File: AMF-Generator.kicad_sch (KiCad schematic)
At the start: 37 parts, among them J1 SW_OUT, J2 CUR_SENSE, J3 PWR_IN, Q1 ISC012N04LM6ATMA1, Q2 ISC012N04LM6ATMA1, U1 ACS732KLATR-75AB, U2 UCC21540, U8 74LVC1G06

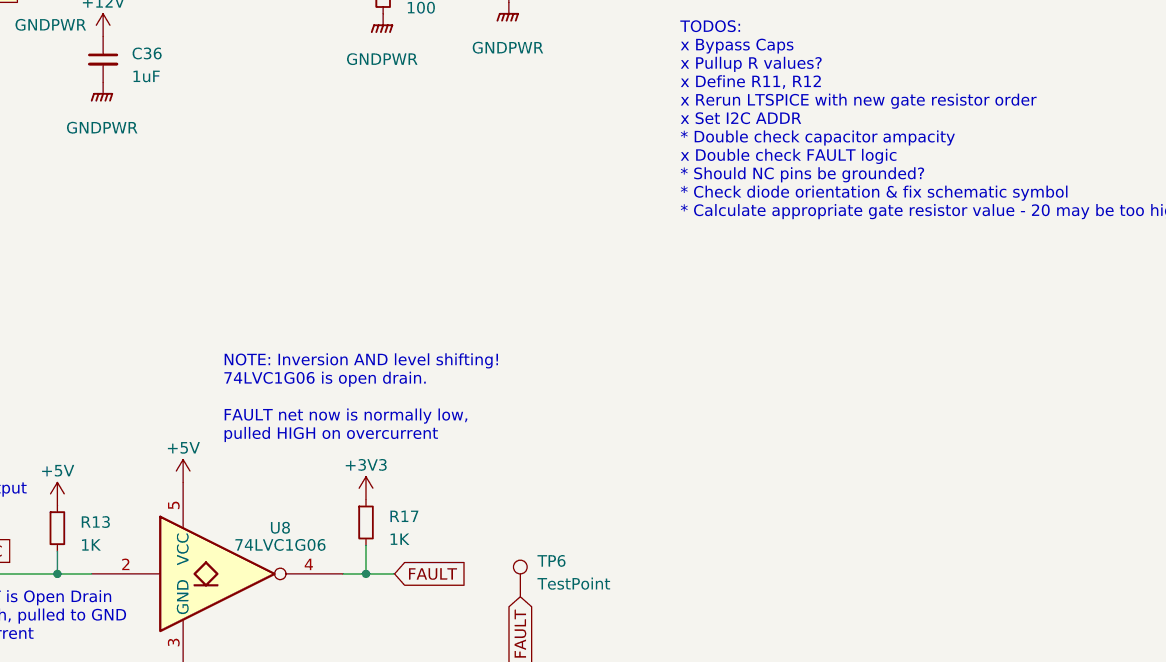
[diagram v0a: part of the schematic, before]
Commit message: Added bypass cap to inverter and some cleanup
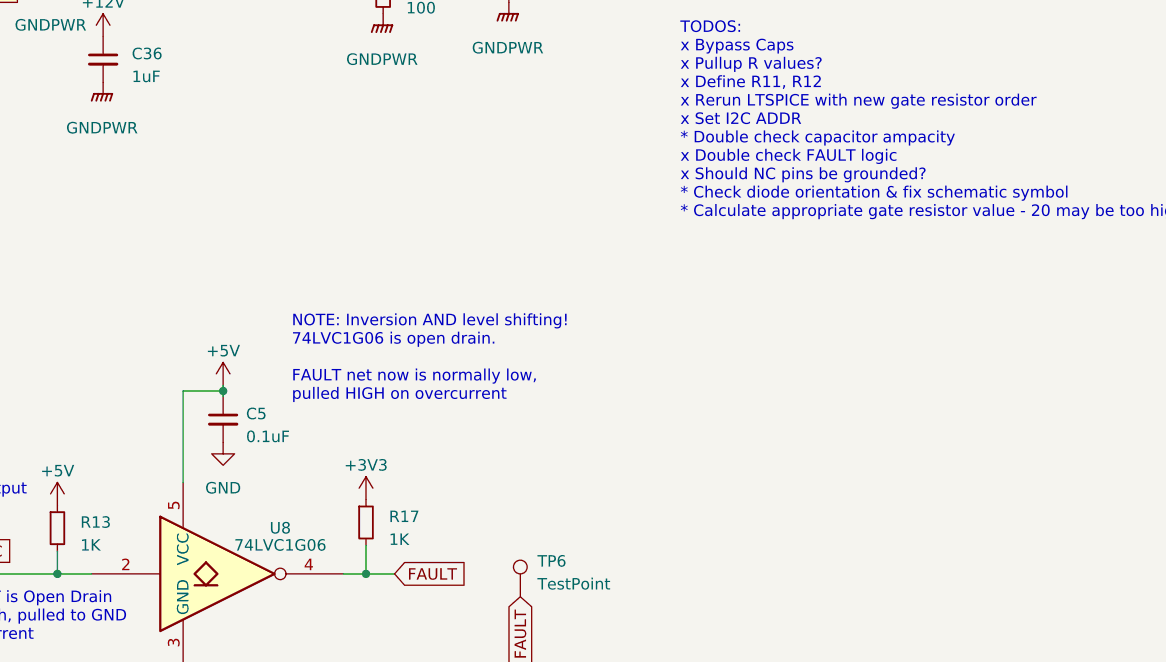
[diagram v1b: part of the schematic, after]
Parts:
- added C5: 0.1uF, Capacitor_SMD:C_0805_2012Metric, symbol Device:C_Small
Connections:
- net +5V: now also C5.1
- net GND: now also C5.2
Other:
- note added: "TODOS: x Bypass Caps x Pullup R values? x Define R11, R12 x Rerun LTSPICE with new gate resistor order x Set I2C ADDR * Double check capacitor ampacity x Double check FAULT logic x Should NC pins be grounded? * Check diode orientation & fix schematic symbol * Calculate appropriate gate resistor value - 20 may be too high"
- note removed: "TODOS: x Bypass Caps x Pullup R values? x Define R11, R12 x Rerun LTSPICE with new gate resistor order x Set I2C ADDR * Double check capacitor ampacity x Double check FAULT logic * Should NC pins be grounded? * Check diode orientation & fix schematic symbol * Calculate appropriate gate resistor value - 20 may be too high"
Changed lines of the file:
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@@
   (junction (at 121.285 166.37) (diameter 0) (color 0 0 0 0)
   )
+  (junction (at 105.41 146.05) (diameter 0) (color 0 0 0 0)
+  )
   (junction (at 143.51 77.47) (diameter 0) (color 0 0 0 0)
   )
@@
     (stroke (width 0) (type default))
   )
+  (wire (pts (xy 100.965 156.21) (xy 100.965 146.05))
+    (stroke (width 0) (type default))
+  )
   (wire (pts (xy 130.81 72.39) (xy 132.08 72.39))
     (stroke (width 0) (type default))
@@
     (stroke (width 0) (type default))
   )
+  (wire (pts (xy 105.41 146.05) (xy 105.41 146.685))
+    (stroke (width 0) (type default))
+  )
   (wire (pts (xy 178.435 77.47) (xy 178.435 69.85))
     (stroke (width 0) (type default))
@@
     (stroke (width 0) (type default))
   )
+  (wire (pts (xy 100.965 146.05) (xy 105.41 146.05))
+    (stroke (width 0) (type default))
+  )
   (wire (pts (xy 123.19 97.79) (xy 129.54 97.79))
     (stroke (width 0) (type default))
@@
   )
   (wire (pts (xy 60.325 140.97) (xy 60.325 153.67))
+    (stroke (width 0) (type default))
+  )
+  (wire (pts (xy 105.41 145.415) (xy 105.41 146.05))
     (stroke (width 0) (type default))
   )
@@
     (effects (font (size 1.27 1.27)) (justify left bottom))
   )
-  (text "TODOS:\nx Bypass Caps\nx Pullup R values?\nx Define R11, R12\nx Rerun LTSPICE with new gate resistor order\nx Set I2C ADDR\n* Double check capacitor ampacity\nx Double check FAULT logic\n* Should NC pins be grounded?\n* Check diode orientation & fix schematic symbol\n* Calculate appropriate gate resistor value - 20 may be too high"
+  (text "TODOS:\nx Bypass Caps\nx Pullup R values?\nx Define R11, R12\nx Rerun LTSPICE with new gate resistor order\nx Set I2C ADDR\n* Double check capacitor ampacity\nx Double check FAULT logic\nx Should NC pins be grounded?\n* Check diode orientation & fix schematic symbol\n* Calculate appropriate gate resistor value - 20 may be too high"
     (at 156.21 127 0)
     (effects (font (size 1.27 1.27)) (justify left bottom))
@@
   )
   (text "NOTE: Inversion AND level shifting!\n74LVC1G06 is open drain.\n\nFAULT net now is normally low,\npulled HIGH on overcurrent"
-    (at 105.41 151.765 0)
+    (at 113.03 147.32 0)
     (effects (font (size 1.27 1.27)) (justify left bottom))
   )
@@
         (path "/c3df021c-646c-4a68-ac14-a081c2121d02"
           (reference "#PWR069") (unit 1)
+        )
+      )
+    )
+  )
+  (symbol (lib_id "power:GND") (at 105.41 151.765 0) (unit 1)
+    (in_bom yes) (on_board yes) (dnp no) (fields_autoplaced)
+    (property "Reference" "#PWR065" (at 105.41 158.115 0)
+      (effects (font (size 1.27 1.27)) hide)
+    )
+    (property "Value" "GND" (at 105.41 156.845 0)
+      (effects (font (size 1.27 1.27)))
+    )
+    (property "Footprint" "" (at 105.41 151.765 0)
+      (effects (font (size 1.27 1.27)) hide)
+    )
+    (property "Datasheet" "" (at 105.41 151.765 0)
+      (effects (font (size 1.27 1.27)) hide)
+    )
+    (pin "1")
+    (instances
+      (project "AMF-Generator"
+        (path "/c3df021c-646c-4a68-ac14-a081c2121d02"
+          (reference "#PWR065") (unit 1)
         )
       )
@@
         (path "/c3df021c-646c-4a68-ac14-a081c2121d02"
           (reference "#FLG01") (unit 1)
-        )
-      )
-    )
-  )
-  (symbol (lib_id "power:+5V") (at 100.965 156.21 0) (unit 1)
-    (in_bom yes) (on_board yes) (dnp no) (fields_autoplaced)
-    (property "Reference" "#PWR078" (at 100.965 160.02 0)
-      (effects (font (size 1.27 1.27)) hide)
-    )
-    (property "Value" "+5V" (at 100.965 152.4 0)
-      (effects (font (size 1.27 1.27)))
-    )
-    (property "Footprint" "" (at 100.965 156.21 0)
-      (effects (font (size 1.27 1.27)) hide)
-    )
-    (property "Datasheet" "" (at 100.965 156.21 0)
-      (effects (font (size 1.27 1.27)) hide)
-    )
-    (pin "1")
-    (instances
-      (project "AMF-Generator"
-        (path "/c3df021c-646c-4a68-ac14-a081c2121d02"
-          (reference "#PWR078") (unit 1)
         )
       )
@@
     )
   )
+  (symbol (lib_id "Device:C_Small") (at 105.41 149.225 0) (unit 1)
+    (in_bom yes) (on_board yes) (dnp no) (fields_autoplaced)
+    (property "Reference" "C5" (at 107.95 148.5963 0)
+      (effects (font (size 1.27 1.27)) (justify left))
+    )
+    (property "Value" "0.1uF" (at 107.95 151.1363 0)
+      (effects (font (size 1.27 1.27)) (justify left))
+    )
+    (property "Footprint" "Capacitor_SMD:C_0805_2012Metric" (at 105.41 149.225 0)
+      (effects (font (size 1.27 1.27)) hide)
+    )
+    (property "Datasheet" "~" (at 105.41 149.225 0)
+      (effects (font (size 1.27 1.27)) hide)
+    )
+    (pin "1")
+    (pin "2")
+    (instances
+      (project "AMF-Generator"
+        (path "/c3df021c-646c-4a68-ac14-a081c2121d02"
+          (reference "C5") (unit 1)
+        )
+      )
+    )
+  )
   (symbol (lib_id "power:GNDPWR") (at 92.075 111.76 0) (unit 1)
     (in_bom yes) (on_board yes) (dnp no) (fields_autoplaced)
@@
         )
       )
+    )
+  )
+  (symbol (lib_id "power:+5V") (at 105.41 145.415 0) (unit 1)
+    (in_bom yes) (on_board yes) (dnp no) (fields_autoplaced)
+    (property "Reference" "#PWR064" (at 105.41 149.225 0)
+      (effects (font (size 1.27 1.27)) hide)
+    )
+    (property "Value" "+5V" (at 105.41 141.605 0)
+      (effects (font (size 1.27 1.27)))
+    )
+    (property "Footprint" "" (at 105.41 145.415 0)
+      (effects (font (size 1.27 1.27)) hide)
+    )
+    (property "Datasheet" "" (at 105.41 145.415 0)
+      (effects (font (size 1.27 1.27)) hide)
+    )
+    (pin "1")
+    (instances
+      (project "AMF-Generator"
+        (path "/c3df021c-646c-4a68-ac14-a081c2121d02"
+          (reference "#PWR064") (unit 1)
+        )
+      )

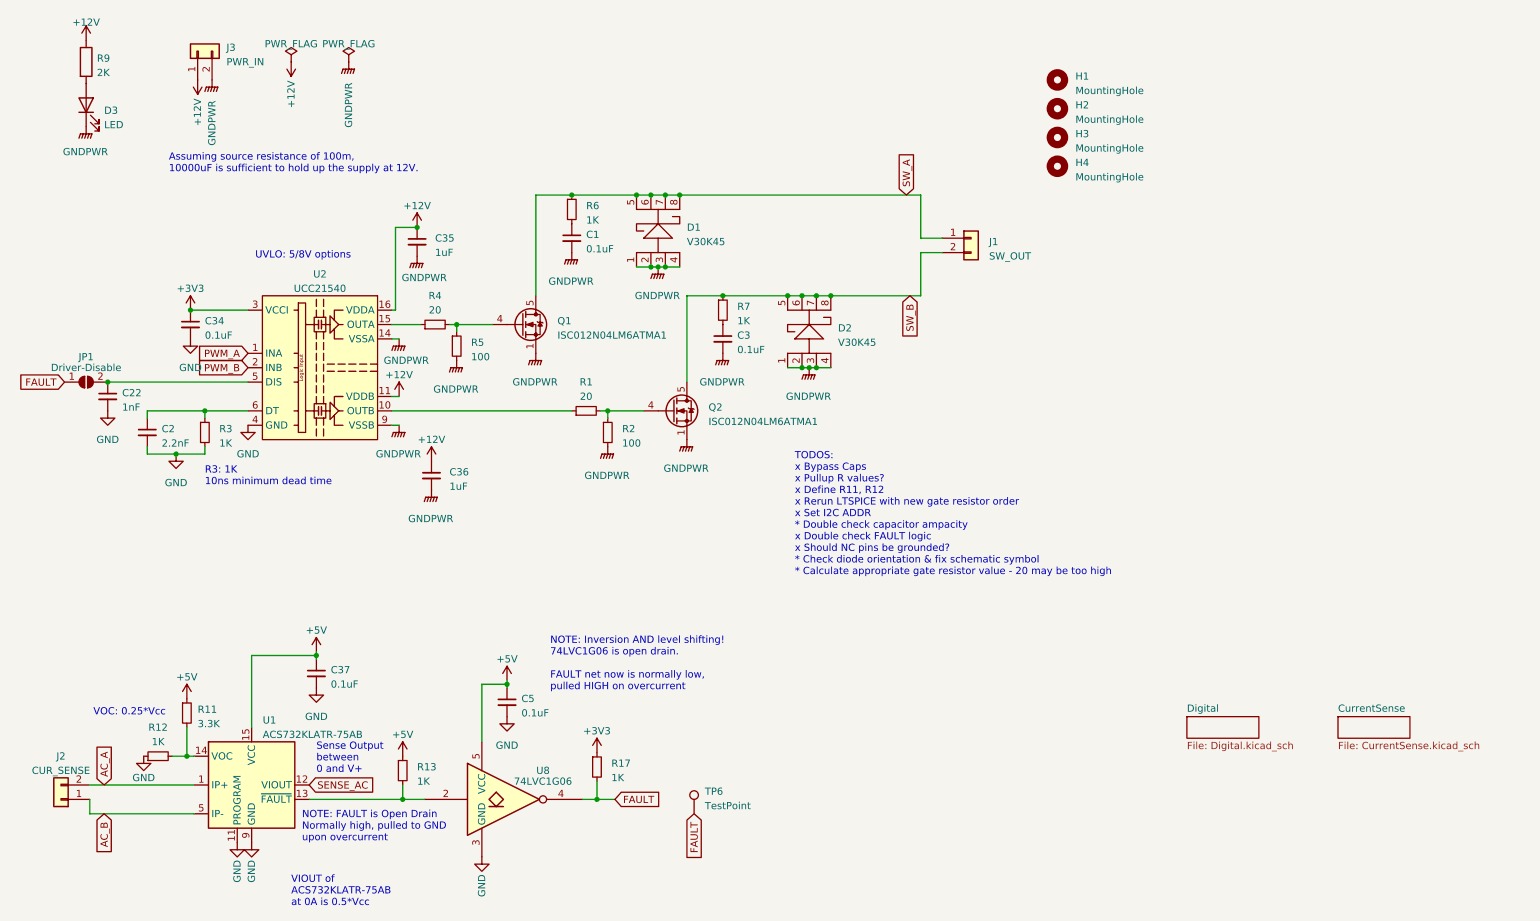
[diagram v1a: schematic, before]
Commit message: Update to improved barrier block and cap bank pcb nearly done
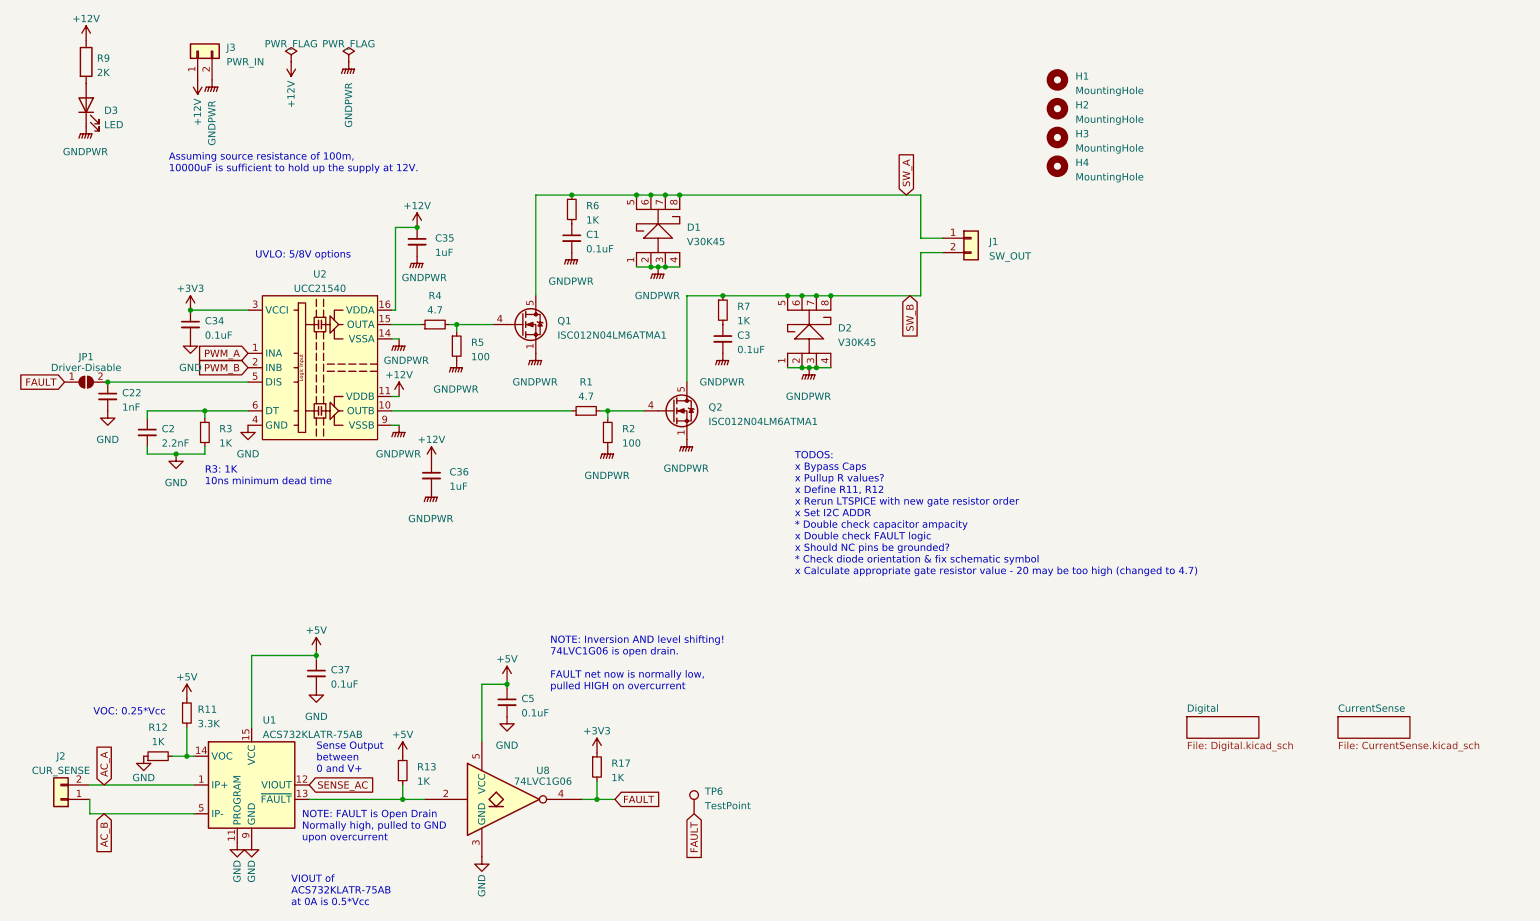
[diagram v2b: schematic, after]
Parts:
- J1, J2: footprint 8PCV-02-006:8PCV02006 -> BarrierBlock:0389690002
- R1, R4: value 20 -> 4.7
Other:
- note added: "TODOS: x Bypass Caps x Pullup R values? x Define R11, R12 x Rerun LTSPICE with new gate resistor order x Set I2C ADDR * Double check capacitor ampacity x Double check FAULT logic x Should NC pins be grounded? * Check diode orientation & fix schematic symbol x Calculate appropriate gate resistor value - 20 may be too high (changed to 4.7)"
- note removed: "TODOS: x Bypass Caps x Pullup R values? x Define R11, R12 x Rerun LTSPICE with new gate resistor order x Set I2C ADDR * Double check capacitor ampacity x Double check FAULT logic x Should NC pins be grounded? * Check diode orientation & fix schematic symbol * Calculate appropriate gate resistor value - 20 may be too high"
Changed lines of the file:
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@@
     (effects (font (size 1.27 1.27)) (justify left bottom))
   )
-  (text "TODOS:\nx Bypass Caps\nx Pullup R values?\nx Define R11, R12\nx Rerun LTSPICE with new gate resistor order\nx Set I2C ADDR\n* Double check capacitor ampacity\nx Double check FAULT logic\nx Should NC pins be grounded?\n* Check diode orientation & fix schematic symbol\n* Calculate appropriate gate resistor value - 20 may be too high"
+  (text "TODOS:\nx Bypass Caps\nx Pullup R values?\nx Define R11, R12\nx Rerun LTSPICE with new gate resistor order\nx Set I2C ADDR\n* Double check capacitor ampacity\nx Double check FAULT logic\nx Should NC pins be grounded?\n* Check diode orientation & fix schematic symbol\nx Calculate appropriate gate resistor value - 20 may be too high (changed to 4.7)"
     (at 156.21 127 0)
     (effects (font (size 1.27 1.27)) (justify left bottom))
@@
   )
   (symbol (lib_id "power:+12V") (at 31.115 32.385 0) (unit 1)
-    (in_bom yes) (on_board yes) (dnp no) (fields_autoplaced)
+    (in_bom yes) (on_board yes) (dnp no)
     (property "Reference" "#PWR069" (at 31.115 36.195 0)
       (effects (font (size 1.27 1.27)) hide)
     )
-    (property "Value" "+12V" (at 31.115 29.21 0)
+    (property "Value" "+12V" (at 31.115 28.575 0)
       (effects (font (size 1.27 1.27)))
     )
@@
       (effects (font (size 1.27 1.27)) (justify left))
     )
-    (property "Footprint" "8PCV-02-006:8PCV02006" (at 187.325 67.31 0)
+    (property "Footprint" "BarrierBlock:0389690002" (at 187.325 67.31 0)
       (effects (font (size 1.27 1.27)) hide)
     )
@@
       (effects (font (size 1.27 1.27)))
     )
-    (property "Value" "20" (at 119.38 95.25 90)
+    (property "Value" "4.7" (at 119.38 95.25 90)
       (effects (font (size 1.27 1.27)))
     )
@@
       (effects (font (size 1.27 1.27)))
     )
-    (property "Value" "20" (at 92.71 80.01 90)
+    (property "Value" "4.7" (at 92.71 80.01 90)
       (effects (font (size 1.27 1.27)))
     )
@@
       (effects (font (size 1.27 1.27)))
     )
-    (property "Footprint" "8PCV-02-006:8PCV02006" (at 26.67 166.37 0)
-      (effects (font (size 1.27 1.27)) hide)
-    )
+    (property "Footprint" "BarrierBlock:0389690002" (at 26.67 166.37 0)
+      (effects (font (size 1.27 1.27)) hide)
+    )

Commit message: cleanup
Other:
- note added: "Assuming source resistance of 100m, 10000uF is sufficient to hold up the supply at 12V. Not onboard! Needs to be provided externally."
- note added: "UVLO: 5/8V options PWMA, PWMB internally pulled low"
- note removed: "Assuming source resistance of 100m, 10000uF is sufficient to hold up the supply at 12V."
- note removed: "UVLO: 5/8V options"
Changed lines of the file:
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@@
     (effects (font (size 1.27 1.27)) (justify left bottom))
   )
-  (text "Assuming source resistance of 100m,\n10000uF is sufficient to hold up the supply at 12V."
-    (at 45.72 55.88 0)
+  (text "Assuming source resistance of 100m,\n10000uF is sufficient to hold up the supply at 12V.\nNot onboard! Needs to be provided externally."
+    (at 45.72 57.785 0)
     (effects (font (size 1.27 1.27)) (justify left bottom))
   )
-  (text "UVLO: 5/8V options" (at 60.96 71.12 0)
+  (text "UVLO: 5/8V options\nPWMA, PWMB internally\npulled low"
+    (at 59.69 71.755 0)
     (effects (font (size 1.27 1.27)) (justify left bottom))
   )
